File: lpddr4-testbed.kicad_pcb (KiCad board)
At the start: 6 copper layers, 69.6 x 30 mm, 44 parts, among them J1 ddr4-sodimm-edge-connector, U1 MT53E256M16D1

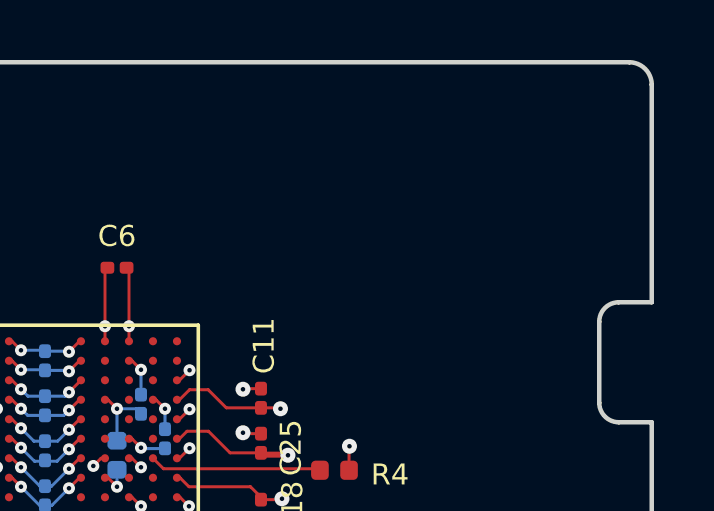
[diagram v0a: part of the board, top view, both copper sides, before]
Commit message: Add OSHW logotype
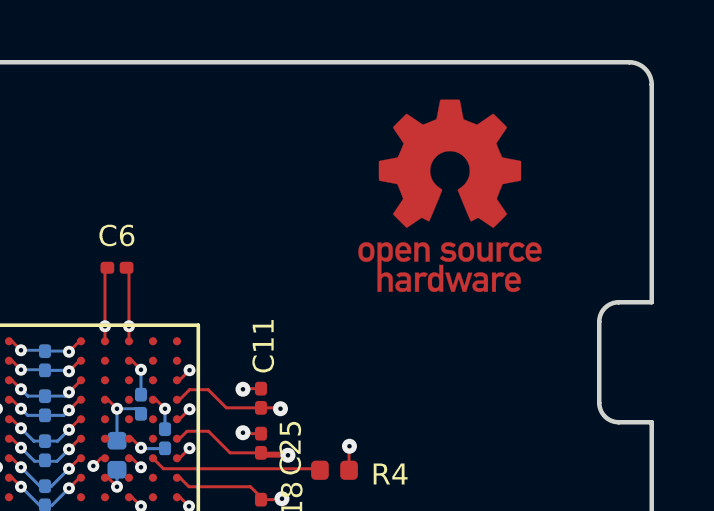
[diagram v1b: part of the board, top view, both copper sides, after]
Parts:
- added N1: oshw_logo, antmicro-footprints:oshw-logo, F.Cu at (162.9, 74.5)

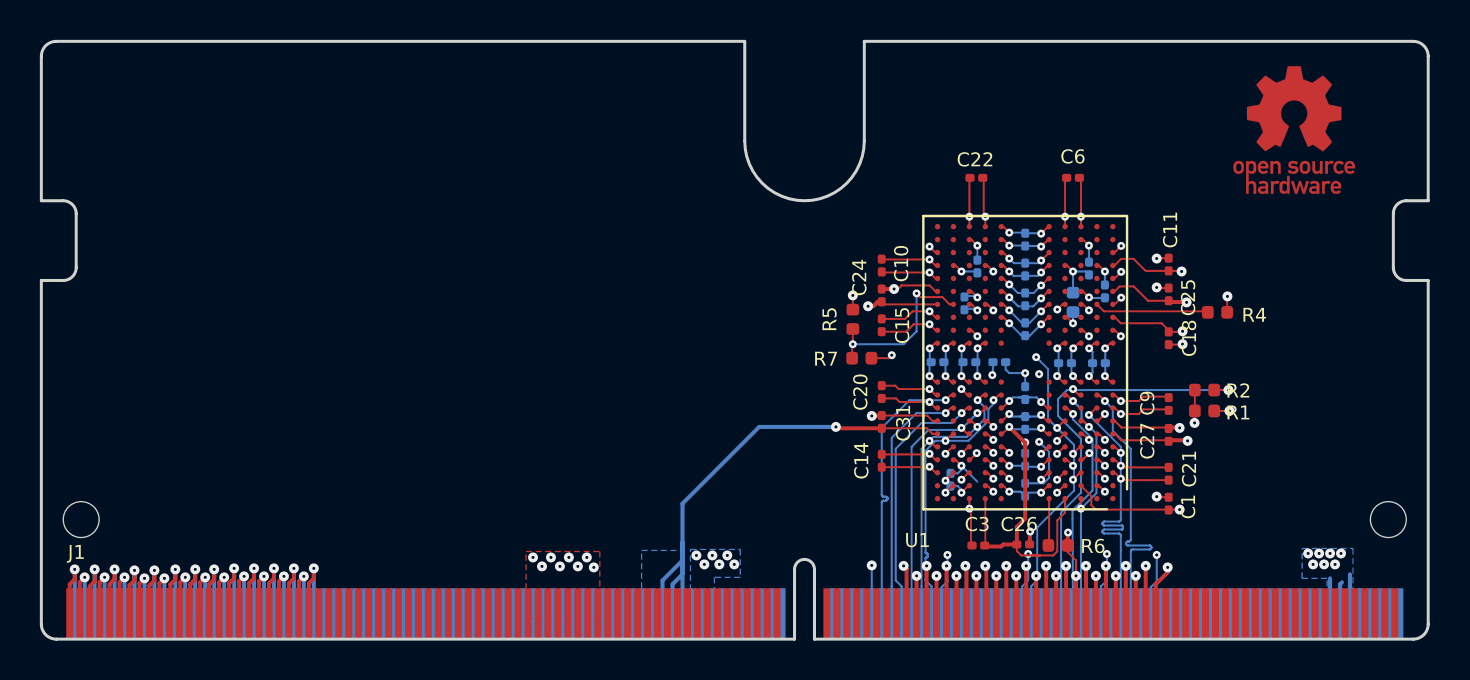
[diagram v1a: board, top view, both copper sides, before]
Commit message: Optimize pairs of buried vias
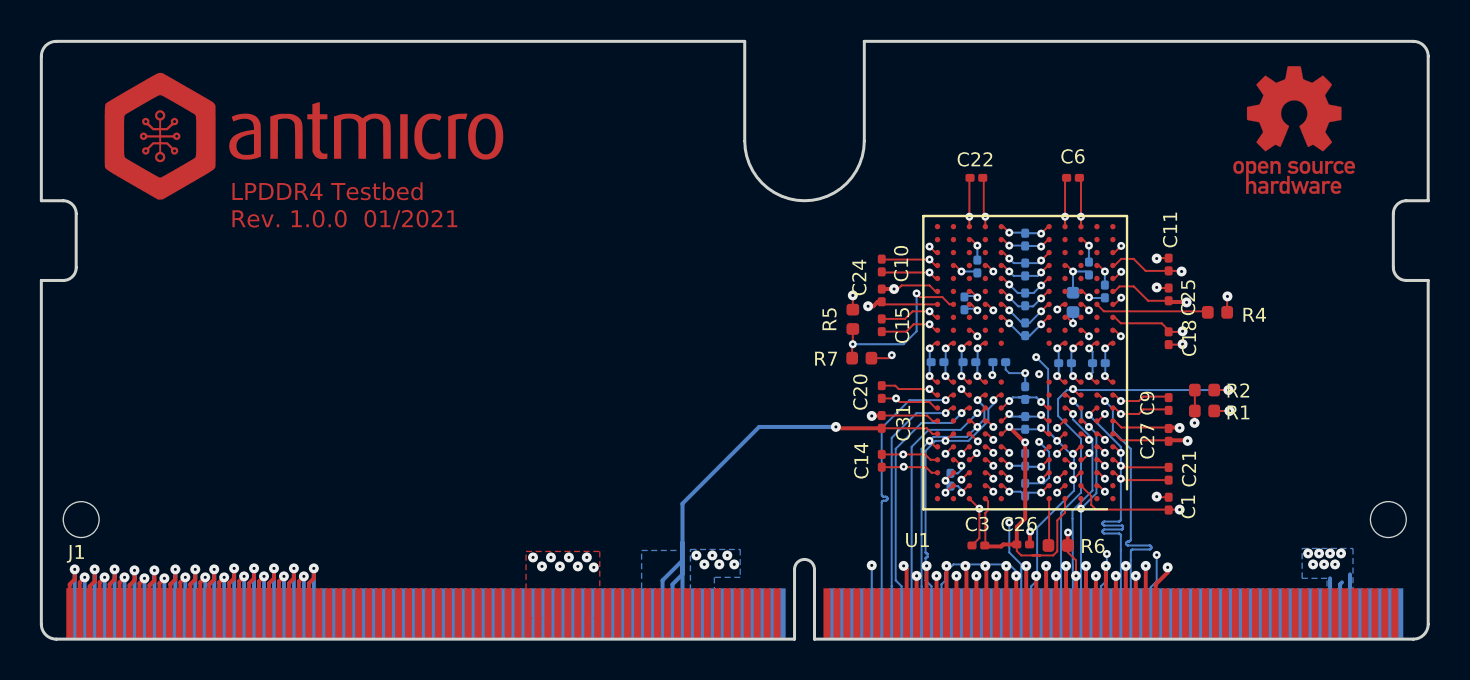
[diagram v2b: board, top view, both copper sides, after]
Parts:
- added N1: antmicro_logo, antmicro-footprints:antmicro-logo_scaled_20mm, F.Cu at (113.2, 75.0)
- renumbered N1 to N3
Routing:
- net GND: track 220.5 -> 224.7 mm, vias 101 -> 100
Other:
- net class Default: via_dia 0.5 -> 0.4
- board text added: "LPDDR4 Testbed Rev. 1.0.0 01/2021"

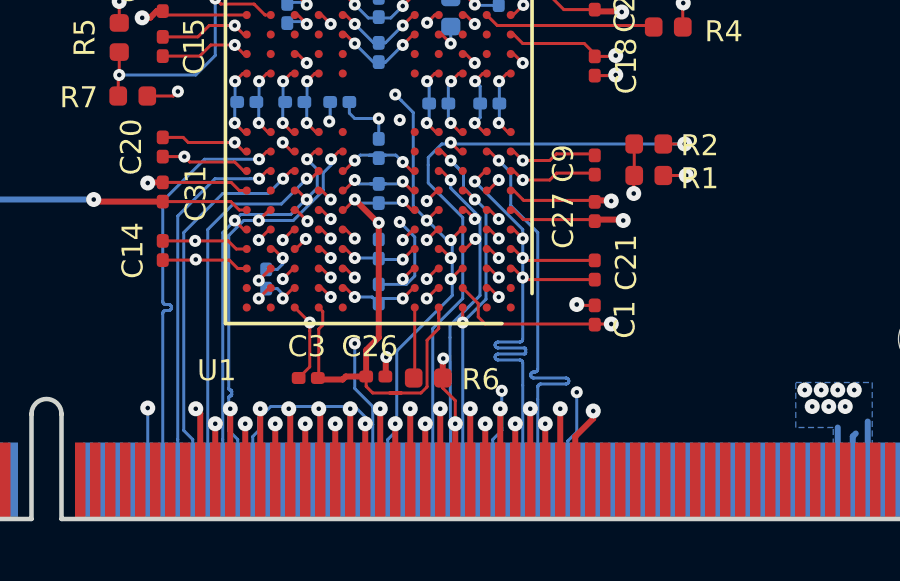
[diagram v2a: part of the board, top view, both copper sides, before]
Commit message: Update local libs, resolve DRC
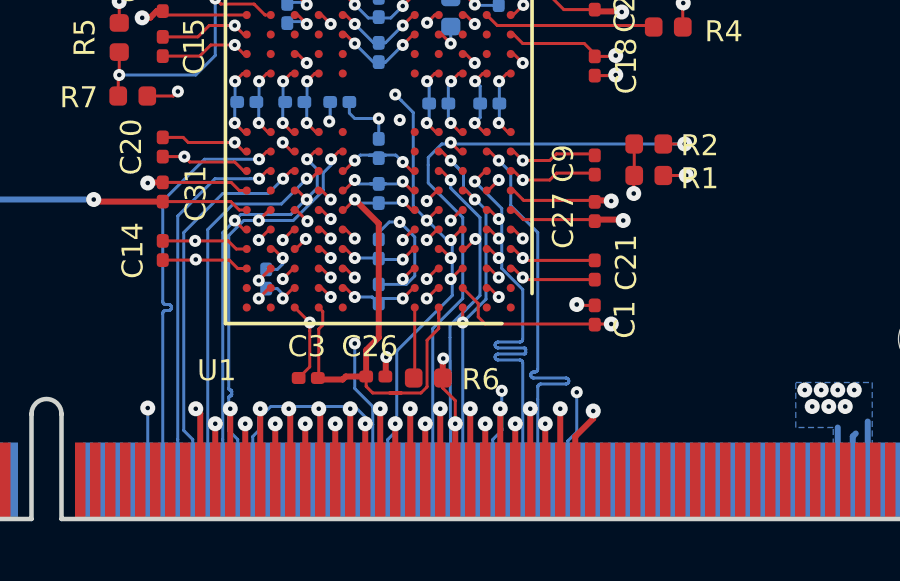
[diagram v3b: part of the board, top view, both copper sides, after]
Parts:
- C1, C10, C11, C12, C13, C14, C15, C16, C17, C18, C19, C2, C20, C21, C22, C23, C24, C25, C26, C27, C28, C29, C3, C30, C31, C32, C33, C35, C36, C4, C5, C6, C7, C8, C9: footprint antmicro-footprints:0201-res -> lpddr4-testbed-footprints:0201-res
- J1: footprint antmicro-footprints:SODIMM_DDR4_EDGE -> lpddr4-testbed-footprints:SODIMM_DDR4_EDGE
- N1: footprint antmicro-footprints:antmicro-logo_scaled_20mm -> lpddr4-testbed-footprints:antmicro-logo_scaled_20mm
- N3: footprint antmicro-footprints:oshw-logo -> lpddr4-testbed-footprints:oshw-logo
- R1, R2, R3, R4, R5, R6, R7: footprint antmicro-footprints:0402-res -> lpddr4-testbed-footprints:0402-res
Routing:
- net GND: track 224.7 -> 225.2 mm, vias 100 -> 99

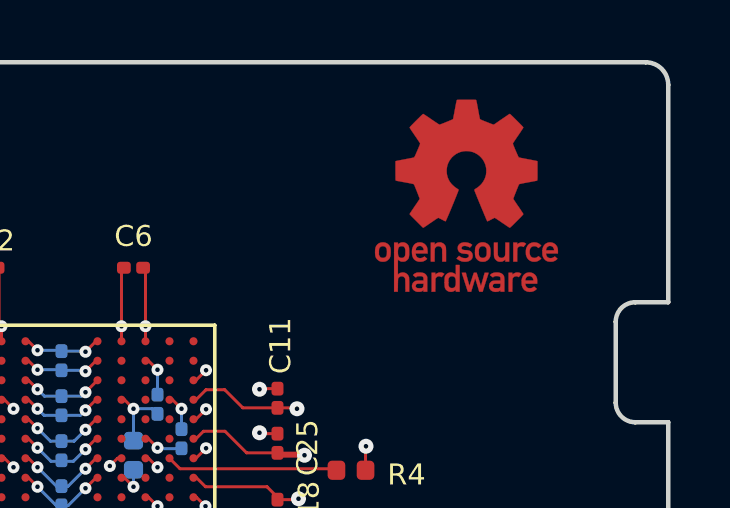
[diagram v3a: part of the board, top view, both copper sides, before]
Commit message: Update DRAM MPN
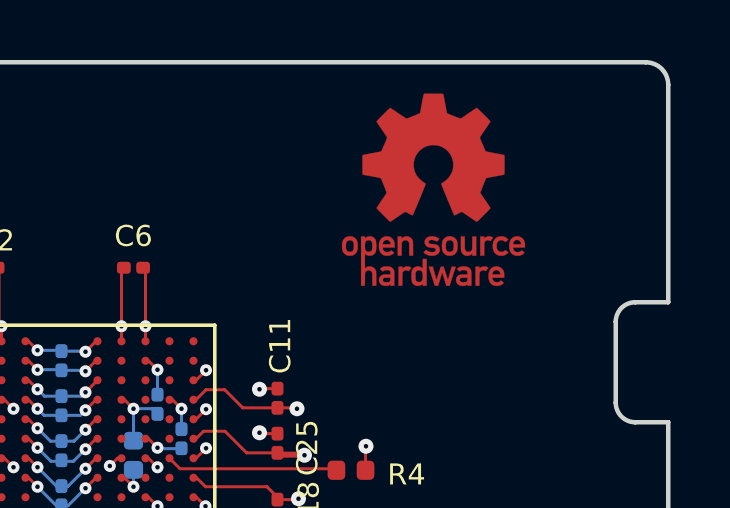
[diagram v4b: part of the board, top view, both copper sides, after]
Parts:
- removed N3: oshw_logo, lpddr4-testbed-footprints:oshw-logo
- added N2: oshw_logo, lpddr4-testbed-footprints:oshw-logo, F.Cu at (161.8, 74.2)
- U1: value MT53E256M16D1 -> MT53E256M32D2DS-053

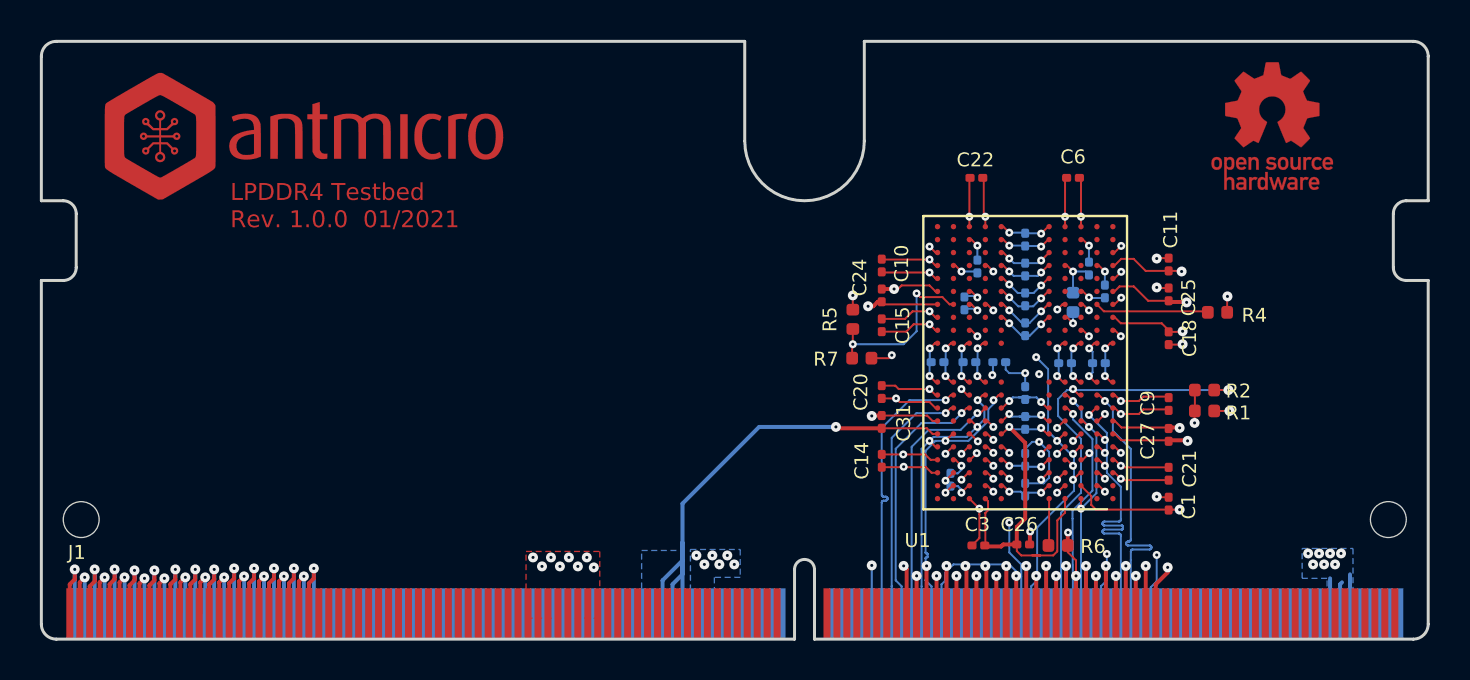
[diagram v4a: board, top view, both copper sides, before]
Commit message: Component placement for EEPROM/LEDs
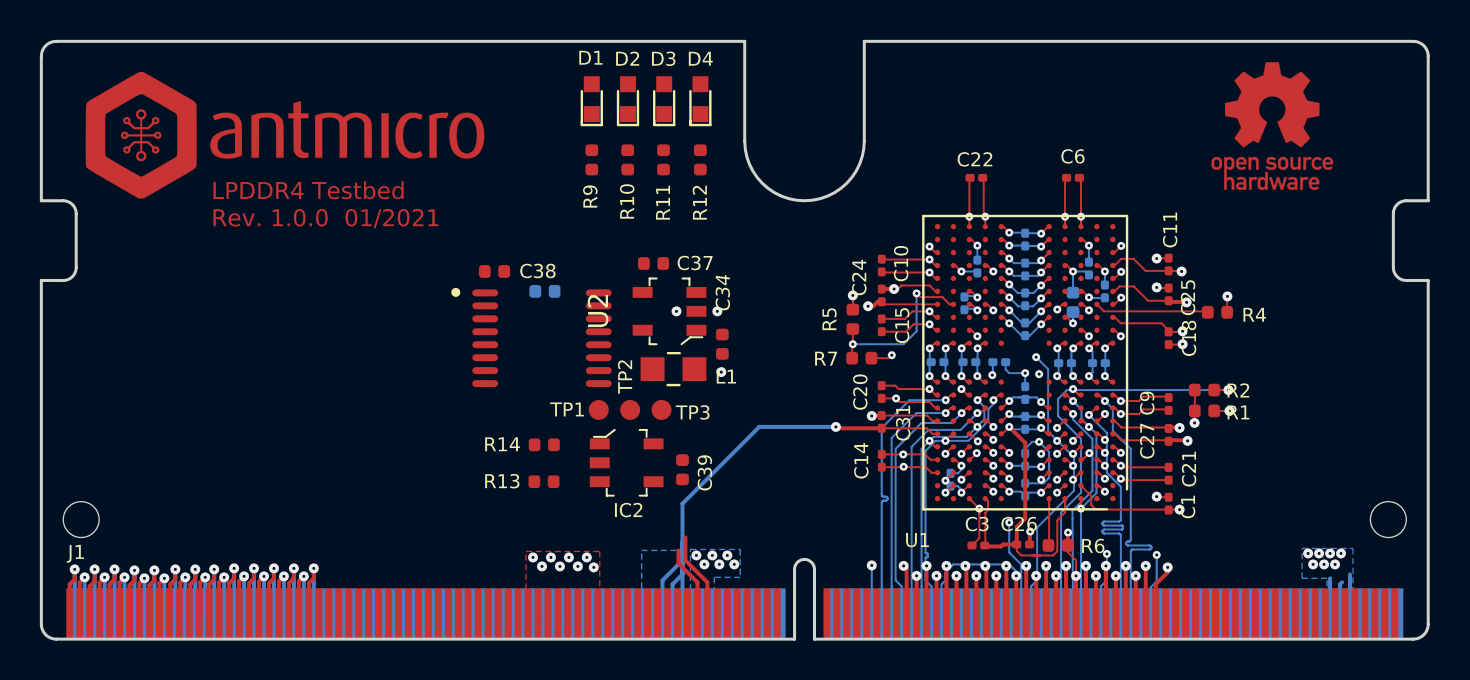
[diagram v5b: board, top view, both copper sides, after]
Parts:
- added C34: C_4u7_0402, lpddr4-testbed-footprints:0402-cap, F.Cu at (134.2, 85.2)
- added C37: C_4u7_0402, lpddr4-testbed-footprints:0402-cap, F.Cu at (130.7, 81.2)
- added C38: C_100n_0402, lpddr4-testbed-footprints:0402-cap, F.Cu at (122.7, 81.5)
- added C39: C_100n_0402, lpddr4-testbed-footprints:0402-cap, F.Cu at (132.2, 91.5)
- added D1: KP-1608CGCK, lpddr4-testbed-footprints:LED_0603, F.Cu at (127.6, 72.9)
- added D2: KP-1608CGCK, lpddr4-testbed-footprints:LED_0603, F.Cu at (129.4, 72.9)
- added D3: KP-1608CGCK, lpddr4-testbed-footprints:LED_0603, F.Cu at (131.3, 72.9)
- added D4: KP-1608CGCK, lpddr4-testbed-footprints:LED_0603, F.Cu at (133.1, 72.9)
- added IC1: PCA96408APW, lpddr4-testbed-footprints:TSSOP-16, F.Cu at (125.1, 84.9)
- added IC2: AT24CS01, lpddr4-testbed-footprints:SOT-23-5, F.Cu at (129.4, 91.2)
- added L1: 1285AS-H-2R2M=P2, lpddr4-testbed-footprints:0805-res, F.Cu at (131.7, 86.5)
- added R10: R_220R_0402, lpddr4-testbed-footprints:0402-res, F.Cu at (129.4, 76.0)
- added R11: R_220R_0402, lpddr4-testbed-footprints:0402-res, F.Cu at (131.2, 76.0)
- added R12: R_220R_0402, lpddr4-testbed-footprints:0402-res, F.Cu at (133.1, 76.0)
- added R13: R_10k_0402, lpddr4-testbed-footprints:0402-res, F.Cu at (125.2, 92.1)
- added R14: R_10k_0402, lpddr4-testbed-footprints:0402-res, F.Cu at (125.2, 90.2)
- added R8: R_0R_0402, lpddr4-testbed-footprints:0402-res, B.Cu at (125.3, 82.5)
- added R9: R_220R_0402, lpddr4-testbed-footprints:0402-res, F.Cu at (127.6, 76.0)
- added TP1: TP_SMD1MM, lpddr4-testbed-footprints:Testpoint_smd_1mm, F.Cu at (128.0, 88.5)
- added TP2: TP_SMD1MM, lpddr4-testbed-footprints:Testpoint_smd_1mm, F.Cu at (129.6, 88.5)
- added TP3: TP_SMD1MM, lpddr4-testbed-footprints:Testpoint_smd_1mm, F.Cu at (131.1, 88.5)
- added U2: TPS613221ADBVT, lpddr4-testbed-footprints:SOT-23-5, F.Cu at (131.5, 83.5)
- moved N1 0.95 mm to (112.2, 74.9)
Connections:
- J1 pad 127: Net-(J1-Pad127) -> SDA
- J1 pad 129: Net-(J1-Pad129) -> SCL
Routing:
- net SCL: track 0.00 -> 4.26 mm
- net SDA: track 0.00 -> 3.54 mm
- net VDD1: vias 10 -> 11
- net GND: vias 99 -> 101

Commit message: Changed DDR type to MT53E1G32D2NP-046 WT:A
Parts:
- U1: value MT53E256M32D2DS-053 -> MT53E1G32D2NP-046

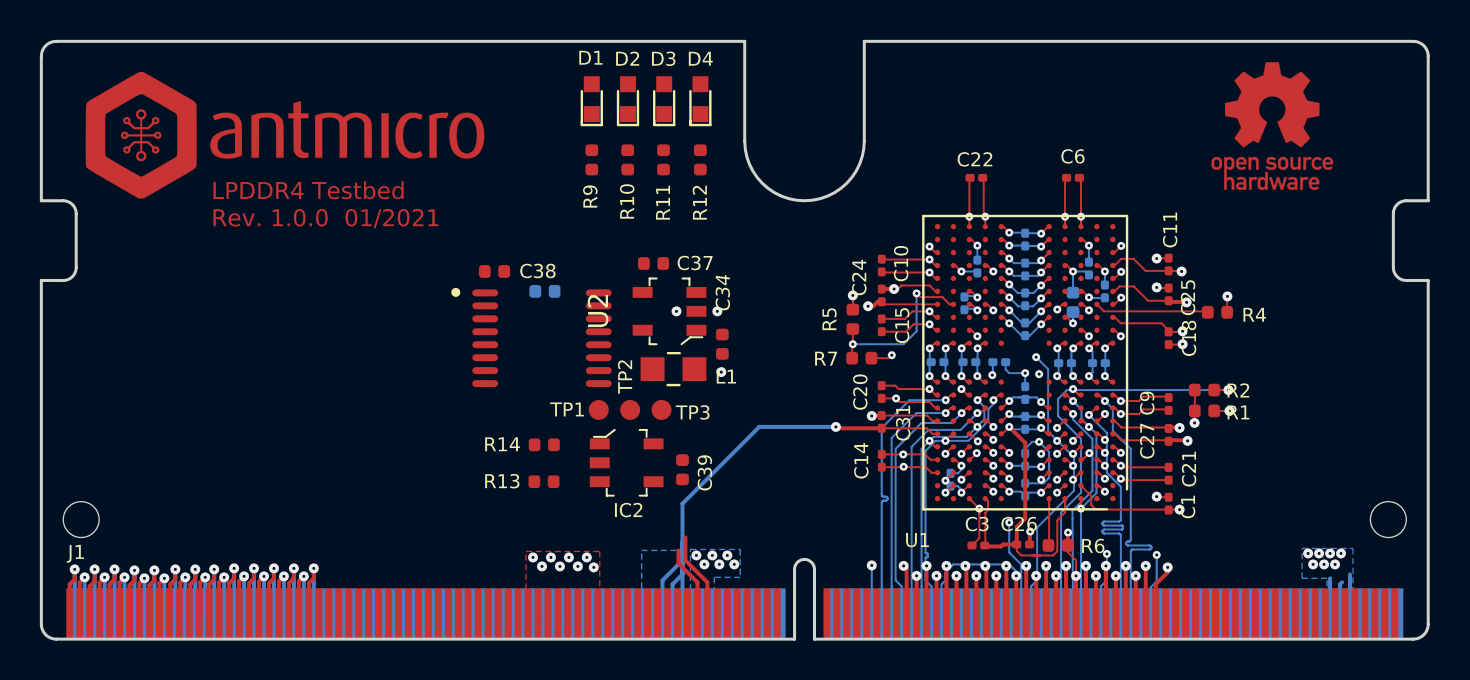
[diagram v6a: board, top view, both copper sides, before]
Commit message: Add eeprom routing
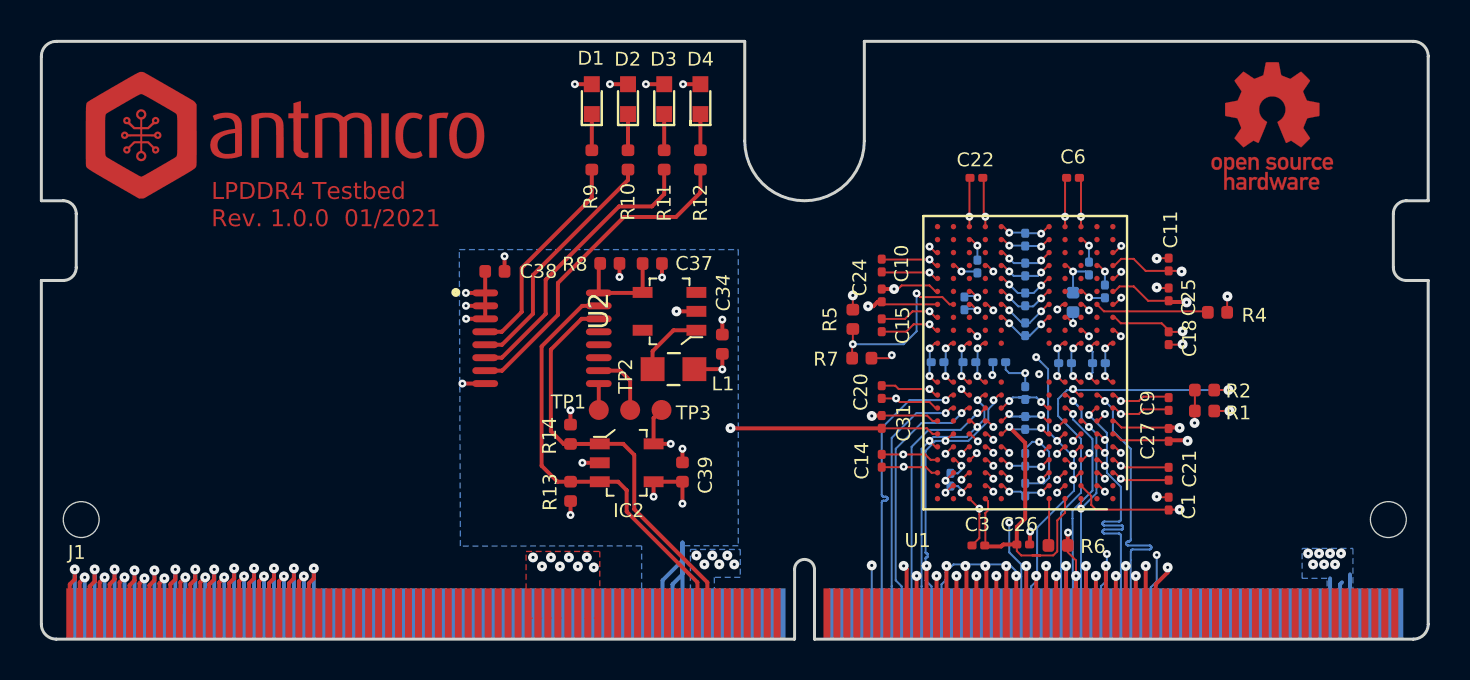
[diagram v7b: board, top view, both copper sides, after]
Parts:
- R8: moved to F.Cu
- moved R8 3.55 mm to (128.5, 81.1), turned to 180 degrees
- moved R13 1.42 mm to (126.6, 92.6), turned to 90 degrees
- moved R14 1.42 mm to (126.6, 89.7), turned to 270 degrees
- moved C39 0.11 mm to (132.2, 91.6)
- moved C37 0.06 mm to (130.7, 81.2)
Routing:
- net SDA: track 3.54 -> 22.1 mm
- net SCL: track 4.26 -> 21.3 mm
- net Net-(IC1-Pad7): track 0.00 -> 16.6 mm
- net Net-(IC1-Pad6): track 0.00 -> 14.6 mm
- net Net-(IC1-Pad5): track 0.00 -> 12.3 mm
- net GND: track 225.2 -> 237.4 mm, vias 101 -> 111
- net VDD1: track 88.4 -> 100.3 mm, vias 11 -> 19
- net Net-(IC1-Pad4): track 0.00 -> 10.8 mm
- net VDDLED: track 0.00 -> 5.17 mm
- net Net-(L1-Pad2): track 0.00 -> 3.53 mm
- net Net-(IC1-Pad10): track 0.00 -> 3.26 mm
- net Net-(D4-Pad1): track 0.00 -> 1.81 mm
- net Net-(D3-Pad1): track 0.00 -> 1.81 mm
- net Net-(D2-Pad1): track 0.00 -> 1.81 mm
- net Net-(D1-Pad1): track 0.00 -> 1.81 mm
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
